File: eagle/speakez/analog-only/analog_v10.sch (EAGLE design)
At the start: 32 parts, among them U1 +12v, U2 MAX5486

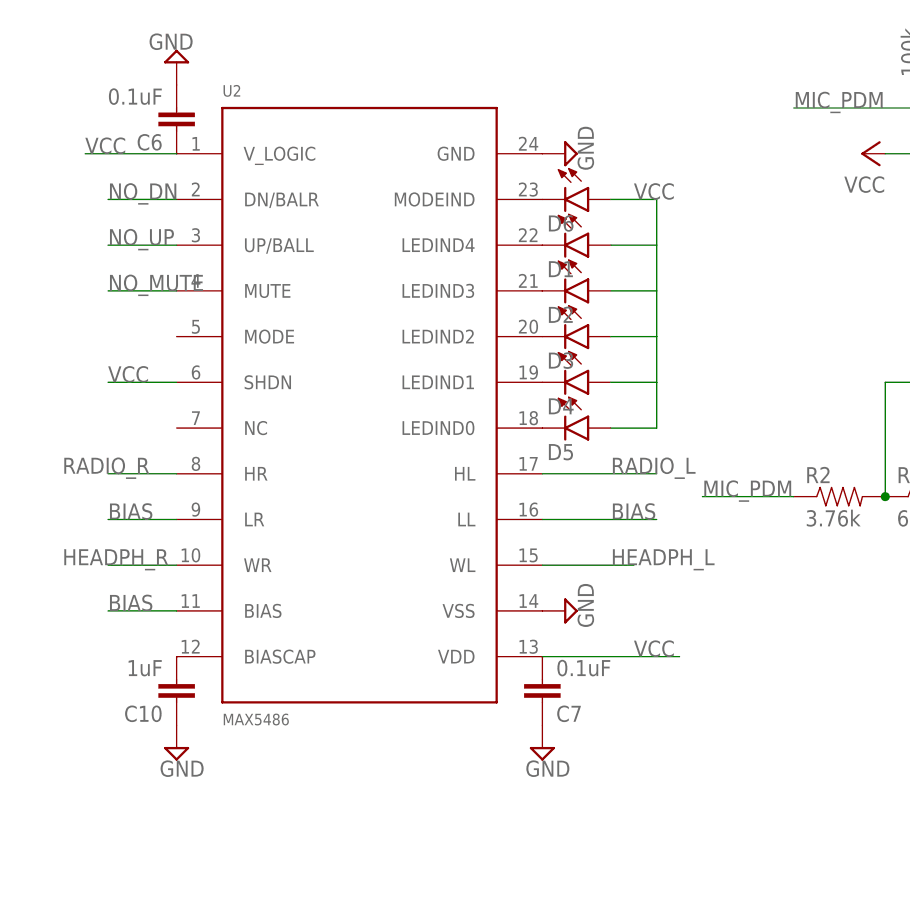
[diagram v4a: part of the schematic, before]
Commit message: got rid of LED, now resistors
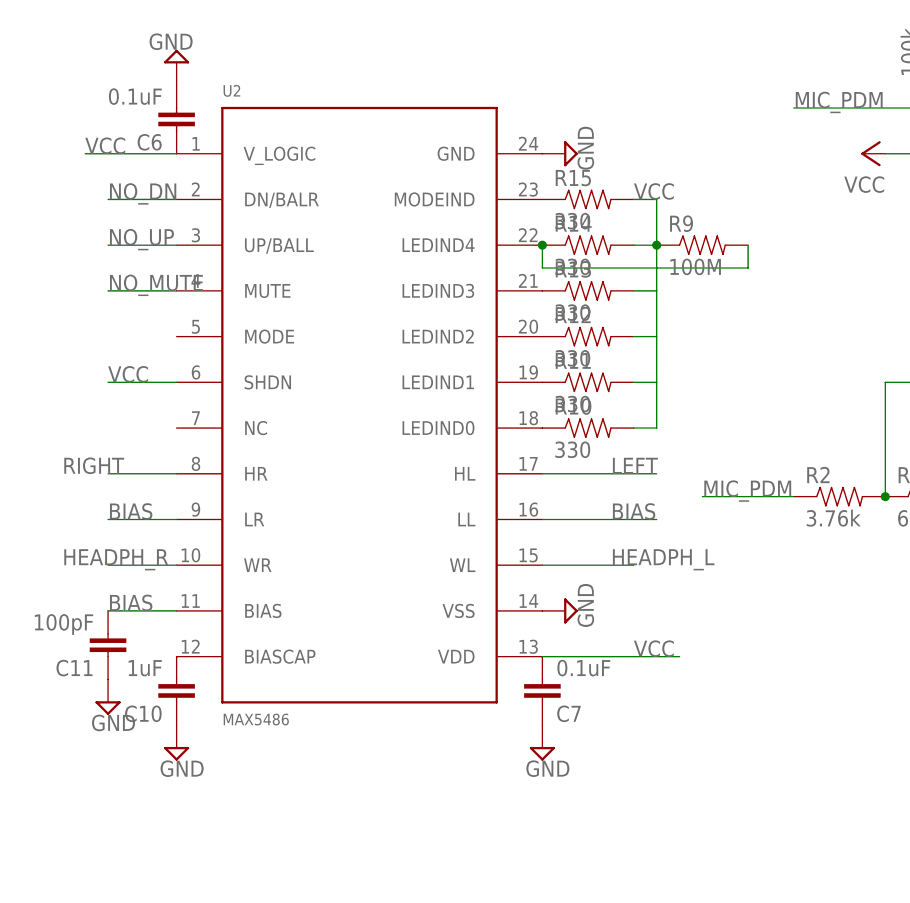
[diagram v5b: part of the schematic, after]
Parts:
- removed D1, D2, D3, D4, D5, D6: (no value), SparkFun-LED:LED1206
- added C11: 100pF, SparkFun-Passives:CAP0805
- added R10, R11, R12, R13, R14, R15: 330, SparkFun-Passives:RESISTOR0805-RES
- added R9: 100M, SparkFun-Passives:RESISTOR0805-RES
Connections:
- removed net N$10: D5.C, U2.LEDIND0
- removed net RADIO_L: U2.HL
- removed net RADIO_R: U2.HR
- new net N$13: R14.1, R9.2, U2.LEDIND4
- net BIAS: now also C11.2
- net GND: now also C11.1
- net LEFT: now also U2.HL
- net N$11: now also R15.1; no longer D6.C
- net N$5: now also R10.1, U2.LEDIND0; no longer D1.C, U2.LEDIND4
- net N$6: now also R11.1, U2.LEDIND1; no longer D2.C, U2.LEDIND3
- net N$8: now also R12.1; no longer D3.C
- net N$9: now also R13.1, U2.LEDIND3; no longer D4.C, U2.LEDIND1
- net RIGHT: now also U2.HR
- net VCC: now also R10.2, R11.2, R12.2, R13.2, R14.2, R15.2, R9.1; no longer D1.A, D2.A, D3.A, D4.A, D5.A, D6.A
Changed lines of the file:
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@@
 <part name="SUPPLY16" library="supply2" deviceset="GND" device=""/>
 <part name="SUPPLY17" library="supply2" deviceset="GND" device=""/>
-<part name="D1" library="SparkFun-LED" deviceset="LED" device="1206"/>
-<part name="D2" library="SparkFun-LED" deviceset="LED" device="1206"/>
-<part name="D3" library="SparkFun-LED" deviceset="LED" device="1206"/>
-<part name="D4" library="SparkFun-LED" deviceset="LED" device="1206"/>
-<part name="D5" library="SparkFun-LED" deviceset="LED" device="1206"/>
-<part name="D6" library="SparkFun-LED" deviceset="LED" device="1206"/>
 <part name="C10" library="SparkFun-Passives" deviceset="CAP" device="0805" value="1uF"/>
 <part name="SUPPLY14" library="supply2" deviceset="GND" device=""/>
+<part name="C11" library="SparkFun-Passives" deviceset="CAP" device="0805" value="100pF"/>
+<part name="SUPPLY15" library="supply2" deviceset="GND" device=""/>
+<part name="R9" library="SparkFun-Passives" deviceset="RESISTOR" device="0805-RES" value="100M"/>
+<part name="R10" library="SparkFun-Passives" deviceset="RESISTOR" device="0805-RES" value="330"/>
+<part name="R11" library="SparkFun-Passives" deviceset="RESISTOR" device="0805-RES" value="330"/>
+<part name="R12" library="SparkFun-Passives" deviceset="RESISTOR" device="0805-RES" value="330"/>
+<part name="R13" library="SparkFun-Passives" deviceset="RESISTOR" device="0805-RES" value="330"/>
+<part name="R14" library="SparkFun-Passives" deviceset="RESISTOR" device="0805-RES" value="330"/>
+<part name="R15" library="SparkFun-Passives" deviceset="RESISTOR" device="0805-RES" value="330"/>
 </parts>
 <sheets>
@@
 <instance part="SUPPLY16" gate="GND" x="-27.94" y="33.02"/>
 <instance part="SUPPLY17" gate="GND" x="-68.58" y="109.22" rot="R180"/>
-<instance part="D1" gate="G$1" x="-22.86" y="88.9" rot="R270"/>
-<instance part="D2" gate="G$1" x="-22.86" y="83.82" rot="R270"/>
-<instance part="D3" gate="G$1" x="-22.86" y="78.74" rot="R270"/>
-<instance part="D4" gate="G$1" x="-22.86" y="73.66" rot="R270"/>
-<instance part="D5" gate="G$1" x="-22.86" y="68.58" rot="R270"/>
-<instance part="D6" gate="G$1" x="-22.86" y="93.98" rot="R270"/>
 <instance part="C10" gate="G$1" x="-68.58" y="40.64" rot="R180"/>
 <instance part="SUPPLY14" gate="GND" x="-68.58" y="33.02"/>
+<instance part="C11" gate="G$1" x="-76.2" y="45.72" rot="R180"/>
+<instance part="SUPPLY15" gate="GND" x="-76.2" y="38.1"/>
+<instance part="R9" gate="G$1" x="-10.16" y="88.9"/>
+<instance part="R10" gate="G$1" x="-22.86" y="68.58"/>
+<instance part="R11" gate="G$1" x="-22.86" y="73.66"/>
+<instance part="R12" gate="G$1" x="-22.86" y="78.74"/>
+<instance part="R13" gate="G$1" x="-22.86" y="83.82"/>
+<instance part="R14" gate="G$1" x="-22.86" y="88.9"/>
+<instance part="R15" gate="G$1" x="-22.86" y="93.98"/>
 </instances>
 <busses>
@@
 <pinref part="C10" gate="G$1" pin="1"/>
 <pinref part="SUPPLY14" gate="GND" pin="GND"/>
+</segment>
+<segment>
+<pinref part="C11" gate="G$1" pin="1"/>
+<pinref part="SUPPLY15" gate="GND" pin="GND"/>
 </segment>
 </net>
@@
 </segment>
 <segment>
-<pinref part="D6" gate="G$1" pin="A"/>
-<wire x1="-20.32" y1="93.98" x2="-15.24" y2="93.98" width="0.1524" layer="91"/>
+<wire x1="-17.78" y1="93.98" x2="-15.24" y2="93.98" width="0.1524" layer="91"/>
 <wire x1="-15.24" y1="93.98" x2="-15.24" y2="88.9" width="0.1524" layer="91"/>
-<pinref part="D5" gate="G$1" pin="A"/>
 <wire x1="-15.24" y1="88.9" x2="-15.24" y2="83.82" width="0.1524" layer="91"/>
 <wire x1="-15.24" y1="83.82" x2="-15.24" y2="78.74" width="0.1524" layer="91"/>
 <wire x1="-15.24" y1="78.74" x2="-15.24" y2="73.66" width="0.1524" layer="91"/>
 <wire x1="-15.24" y1="73.66" x2="-15.24" y2="68.58" width="0.1524" layer="91"/>
-<wire x1="-15.24" y1="68.58" x2="-20.32" y2="68.58" width="0.1524" layer="91"/>
-<pinref part="D4" gate="G$1" pin="A"/>
-<wire x1="-20.32" y1="73.66" x2="-15.24" y2="73.66" width="0.1524" layer="91"/>
-<pinref part="D3" gate="G$1" pin="A"/>
-<wire x1="-20.32" y1="78.74" x2="-15.24" y2="78.74" width="0.1524" layer="91"/>
-<pinref part="D2" gate="G$1" pin="A"/>
-<wire x1="-20.32" y1="83.82" x2="-15.24" y2="83.82" width="0.1524" layer="91"/>
-<pinref part="D1" gate="G$1" pin="A"/>
-<wire x1="-20.32" y1="88.9" x2="-15.24" y2="88.9" width="0.1524" layer="91"/>
+<wire x1="-15.24" y1="68.58" x2="-17.78" y2="68.58" width="0.1524" layer="91"/>
+<wire x1="-17.78" y1="73.66" x2="-15.24" y2="73.66" width="0.1524" layer="91"/>
+<wire x1="-17.78" y1="78.74" x2="-15.24" y2="78.74" width="0.1524" layer="91"/>
+<wire x1="-17.78" y1="83.82" x2="-15.24" y2="83.82" width="0.1524" layer="91"/>
+<wire x1="-17.78" y1="88.9" x2="-15.24" y2="88.9" width="0.1524" layer="91"/>
 <label x="-17.78" y="93.98" size="1.778" layer="95"/>
+<pinref part="R9" gate="G$1" pin="1"/>
+<junction x="-15.24" y="88.9"/>
+<pinref part="R10" gate="G$1" pin="2"/>
+<pinref part="R11" gate="G$1" pin="2"/>
+<pinref part="R12" gate="G$1" pin="2"/>
+<pinref part="R13" gate="G$1" pin="2"/>
+<pinref part="R14" gate="G$1" pin="2"/>
+<pinref part="R15" gate="G$1" pin="2"/>
 </segment>
 </net>
@@
 <label x="93.98" y="-7.62" size="1.778" layer="95" rot="R90"/>
 </segment>
+<segment>
+<pinref part="U2" gate="G$1" pin="HR"/>
+<wire x1="-68.58" y1="63.5" x2="-76.2" y2="63.5" width="0.1524" layer="91"/>
+<label x="-81.28" y="63.5" size="1.778" layer="95"/>
+</segment>
 </net>
 <net name="LEFT" class="0">
@@
 <label x="88.9" y="-7.62" size="1.778" layer="95" rot="R90"/>
 </segment>
+<segment>
+<pinref part="U2" gate="G$1" pin="HL"/>
+<wire x1="-27.94" y1="63.5" x2="-15.24" y2="63.5" width="0.1524" layer="91"/>
+<label x="-20.32" y="63.5" size="1.778" layer="95"/>
+</segment>
 </net>
 <net name="VBATSAFE" class="0">
@@
 <pinref part="VD2" gate="G$1" pin="A"/>
 <wire x1="50.8" y1="119.38" x2="45.72" y2="119.38" width="0.1524" layer="91"/>
-</segment>
-</net>
-<net name="N$5" class="0">
-<segment>
-<pinref part="U2" gate="G$1" pin="LEDIND4"/>
-<pinref part="D1" gate="G$1" pin="C"/>
-</segment>
-</net>
-<net name="N$6" class="0">
-<segment>
-<pinref part="U2" gate="G$1" pin="LEDIND3"/>
-<pinref part="D2" gate="G$1" pin="C"/>
-</segment>
-</net>
-<net name="N$8" class="0">
-<segment>
-<pinref part="U2" gate="G$1" pin="LEDIND2"/>
-<pinref part="D3" gate="G$1" pin="C"/>
-</segment>
-</net>
-<net name="N$9" class="0">
-<segment>
-<pinref part="U2" gate="G$1" pin="LEDIND1"/>
-<pinref part="D4" gate="G$1" pin="C"/>
-</segment>
-</net>
-<net name="N$10" class="0">
-<segment>
-<pinref part="U2" gate="G$1" pin="LEDIND0"/>
-<pinref part="D5" gate="G$1" pin="C"/>
-</segment>
-</net>
-<net name="N$11" class="0">
-<segment>
-<pinref part="U2" gate="G$1" pin="MODEIND"/>
-<pinref part="D6" gate="G$1" pin="C"/>
 </segment>
 </net>
@@
 <wire x1="-68.58" y1="48.26" x2="-76.2" y2="48.26" width="0.1524" layer="91"/>
 <label x="-76.2" y="48.26" size="1.778" layer="95"/>
+<pinref part="C11" gate="G$1" pin="2"/>
 </segment>
 <segment>
@@
 </segment>
 </net>
-<net name="RADIO_R" class="0">
-<segment>
-<pinref part="U2" gate="G$1" pin="HR"/>
-<wire x1="-68.58" y1="63.5" x2="-76.2" y2="63.5" width="0.1524" layer="91"/>
-<label x="-81.28" y="63.5" size="1.778" layer="95"/>
-</segment>
-</net>
-<net name="RADIO_L" class="0">
-<segment>
-<pinref part="U2" gate="G$1" pin="HL"/>
-<wire x1="-27.94" y1="63.5" x2="-15.24" y2="63.5" width="0.1524" layer="91"/>
-<label x="-20.32" y="63.5" size="1.778" layer="95"/>
-</segment>
-</net>
 <net name="NO_DN" class="0">
 <segment>
@@
 </segment>
 </net>
+<net name="N$13" class="0">
+<segment>
+<wire x1="-27.94" y1="86.36" x2="-5.08" y2="86.36" width="0.1524" layer="91"/>
+<pinref part="R9" gate="G$1" pin="2"/>
+<wire x1="-5.08" y1="86.36" x2="-5.08" y2="88.9" width="0.1524" layer="91"/>
+<pinref part="U2" gate="G$1" pin="LEDIND4"/>
+<wire x1="-27.94" y1="88.9" x2="-27.94" y2="86.36" width="0.1524" layer="91"/>
+<pinref part="R14" gate="G$1" pin="1"/>
+<junction x="-27.94" y="88.9"/>
+</segment>
+</net>
+<net name="N$5" class="0">
+<segment>
+<pinref part="U2" gate="G$1" pin="LEDIND0"/>
+<pinref part="R10" gate="G$1" pin="1"/>
+</segment>
+</net>
+<net name="N$6" class="0">
+<segment>
+<pinref part="U2" gate="G$1" pin="LEDIND1"/>
+<pinref part="R11" gate="G$1" pin="1"/>
+</segment>
+</net>
+<net name="N$8" class="0">
+<segment>
+<pinref part="U2" gate="G$1" pin="LEDIND2"/>
+<pinref part="R12" gate="G$1" pin="1"/>
+</segment>
+</net>
+<net name="N$9" class="0">
+<segment>
+<pinref part="U2" gate="G$1" pin="LEDIND3"/>
+<pinref part="R13" gate="G$1" pin="1"/>
+</segment>
+</net>
+<net name="N$11" class="0">
+<segment>
+<pinref part="U2" gate="G$1" pin="MODEIND"/>
+<pinref part="R15" gate="G$1" pin="1"/>
+</segment>
+</net>

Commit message: added zero ohm resistors...just couldn't resist
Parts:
- added C12, C13, C14, C15: 0.1 uF, SparkFun-Passives:CAP0805
- added R16, R17, R21, R22: 1k, SparkFun-Passives:RESISTOR0805-RES
- added R18, R23: 100k, SparkFun-Resistors:RESISTOR0805-RES
- added R19, R20, R24, R25: 1k, SparkFun-Resistors:RESISTOR0805-RES
- added R26, R27: 0, SparkFun-Passives:RESISTOR0805-RES
- added U$4: MCP6L92, Microchip_By_element14_Batch_1:MCP6L92
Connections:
- new net HP_L_AMPD: C15.2, R23.2, R26.1
- new net HP_R_AMPD: C13.2, R18.2, R27.1
- new net N$10: R19.1, R20.1, U$4.VINB-
- new net N$14: R24.1, R25.1, U$4.VINA+
- net GND: now also C12.1, C14.1, R17.1, R18.1, R22.1, R23.1
- net HEADPH_L: now also R25.2
- net HEADPH_R: now also R20.2
- net LEFT: now also R26.2
- net VCC: now also C12.2, C14.2, R16.2, R21.2, U$4.VDD, U$4.VOUTA
- net VIRT_GND: now also R16.1, R17.2, R21.1, R22.2, U$4.GND, U$4.VINB+
- net VOUT_AMP: now also C13.1, C15.1, R19.2, R24.2, U$4.VINA-, U$4.VOUTB

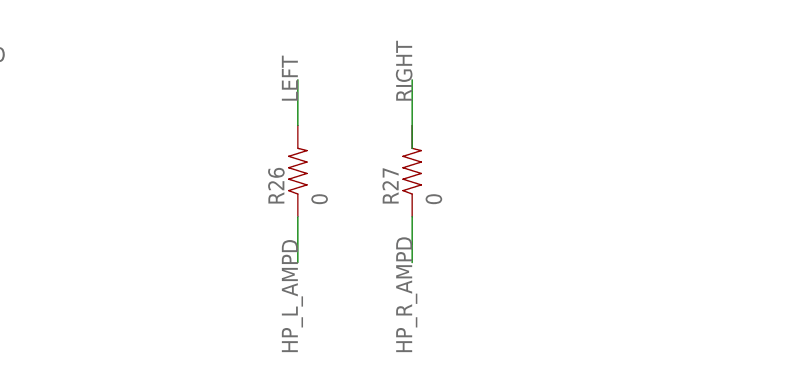
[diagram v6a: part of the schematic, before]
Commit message: resized board
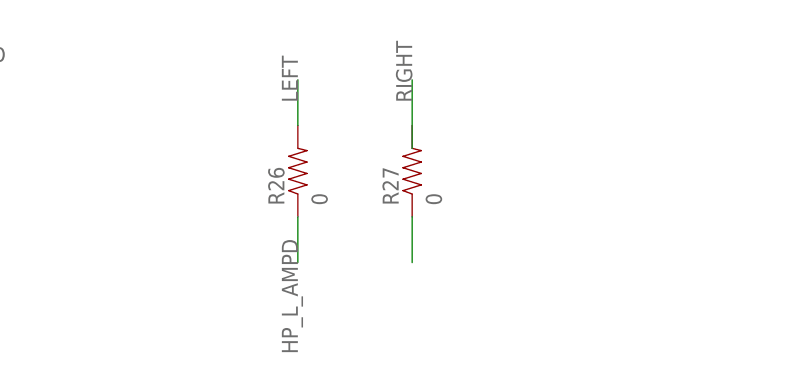
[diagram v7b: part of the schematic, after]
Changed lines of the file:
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@@
 <pinref part="R27" gate="G$1" pin="1"/>
 <wire x1="35.56" y1="-33.02" x2="35.56" y2="-38.1" width="0.1524" layer="91"/>
-<label x="35.56" y="-48.26" size="1.778" layer="95" rot="R90"/>
 </segment>
 </net>

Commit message: all components on, ugly ugly routing
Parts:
- renumbered HEADPHONE to HP
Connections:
- net RIGHT: now also R27.2
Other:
- note added: "AUDIO AMP TO HEADPHONES"
- note added: "BYPASS RESISTORS"
- note added: "MIC FILTER + AMP"
- note added: "MIC OUTPUT"
- note added: "MICROPHONE"
- note added: "OSCILLATOR"
- note added: "RADIO"
- note added: "VOLTAGE REGULATOR"
- note added: "VOLUME CONTROL"
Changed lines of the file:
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@@
 <setting verticaltext="up"/>
 </settings>
-<grid distance="0.1" unitdist="inch" unit="inch" style="lines" multiple="1" display="no" altdistance="0.01" altunitdist="inch" altunit="inch"/>
+<grid distance="0.1" unitdist="inch" unit="inch" style="lines" multiple="1" display="yes" altdistance="0.01" altunitdist="inch" altunit="inch"/>
 <layers>
 <layer number="1" name="Top" color="4" fill="1" visible="yes" active="no"/>
@@
 <part name="C9" library="SparkFun-Passives" deviceset="CAP" device="0805" value="0.1 uF"/>
 <part name="P+5" library="supply1" deviceset="VCC" device=""/>
-<part name="HEADPHONE" library="35mm_audio" deviceset="SJ-43514-SMT" device=""/>
+<part name="HP" library="35mm_audio" deviceset="SJ-43514-SMT" device=""/>
 <part name="RADIO" library="35mm_audio" deviceset="SJ-43514-SMT" device=""/>
 <part name="VD2" library="diode" deviceset="DIODE-SCHOTTKY-" device="SOD123"/>
@@
 <sheet>
 <plain>
+<text x="22.86" y="27.94" size="1.778" layer="91">RADIO</text>
+<text x="81.28" y="27.94" size="1.778" layer="91">MIC OUTPUT</text>
+<text x="20.32" y="-12.7" size="1.778" layer="91">BYPASS RESISTORS</text>
+<text x="-93.98" y="17.78" size="1.778" layer="91">AUDIO AMP TO HEADPHONES</text>
+<text x="-58.42" y="114.3" size="1.778" layer="91">VOLUME CONTROL</text>
+<text x="55.88" y="76.2" size="1.778" layer="91">MIC FILTER + AMP</text>
+<text x="93.98" y="111.76" size="1.778" layer="91">OSCILLATOR</text>
+<text x="20.32" y="127" size="1.778" layer="91">MICROPHONE</text>
+<text x="53.34" y="127" size="1.778" layer="91">VOLTAGE REGULATOR</text>
 </plain>
 <instances>
@@
 <instance part="C9" gate="G$1" x="71.12" y="114.3"/>
 <instance part="P+5" gate="VCC" x="78.74" y="119.38" rot="R270"/>
-<instance part="HEADPHONE" gate="G$1" x="25.4" y="12.7"/>
+<instance part="HP" gate="G$1" x="25.4" y="12.7"/>
 <instance part="RADIO" gate="G$1" x="83.82" y="12.7"/>
 <instance part="VD2" gate="G$1" x="53.34" y="119.38"/>
@@
 </segment>
 <segment>
-<pinref part="HEADPHONE" gate="G$1" pin="SLEEVE"/>
+<pinref part="HP" gate="G$1" pin="SLEEVE"/>
 <wire x1="25.4" y1="7.62" x2="25.4" y2="-5.08" width="0.1524" layer="91"/>
 <label x="25.4" y="-5.08" size="1.778" layer="95" rot="R90"/>
 </segment>
 <segment>
-<pinref part="HEADPHONE" gate="G$1" pin="RING2"/>
+<pinref part="HP" gate="G$1" pin="RING2"/>
 <wire x1="40.64" y1="7.62" x2="40.64" y2="-5.08" width="0.1524" layer="91"/>
 <label x="40.64" y="-5.08" size="1.778" layer="95" rot="R90"/>
@@
 <net name="RIGHT" class="0">
 <segment>
-<pinref part="HEADPHONE" gate="G$1" pin="RING1"/>
+<pinref part="HP" gate="G$1" pin="RING1"/>
 <wire x1="35.56" y1="7.62" x2="35.56" y2="-5.08" width="0.1524" layer="91"/>
 <label x="35.56" y="-5.08" size="1.778" layer="95" rot="R90"/>
@@
 </segment>
 <segment>
-<wire x1="35.56" y1="-25.4" x2="35.56" y2="-17.78" width="0.1524" layer="91"/>
+<pinref part="R27" gate="G$1" pin="2"/>
+<wire x1="35.56" y1="-22.86" x2="35.56" y2="-17.78" width="0.1524" layer="91"/>
 <label x="35.56" y="-20.32" size="1.778" layer="95" rot="R90"/>
 </segment>
@@
 <net name="LEFT" class="0">
 <segment>
-<pinref part="HEADPHONE" gate="G$1" pin="TIP"/>
+<pinref part="HP" gate="G$1" pin="TIP"/>
 <wire x1="30.48" y1="7.62" x2="30.48" y2="-5.08" width="0.1524" layer="91"/>
 <label x="30.48" y="-5.08" size="1.778" layer="95" rot="R90"/>
@@
 <pinref part="R27" gate="G$1" pin="1"/>
 <wire x1="35.56" y1="-33.02" x2="35.56" y2="-38.1" width="0.1524" layer="91"/>
-</segment>
-</net>
+<label x="35.56" y="-48.26" size="1.778" layer="95" rot="R90"/>
+</segment>
+</net>
